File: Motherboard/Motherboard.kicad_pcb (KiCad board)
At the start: 8 copper layers, 304.8 x 243.8 mm, 110 parts, among them J1 ATX-20, J2 65SIB_Connector, J3 DB9_Header, J4 GPIO_Connector, J5 Expansion_Connector, J6 Expansion_Connector, J7 Expansion_Connector, J8 Expansion_Connector, J9 Expansion_Connector, SW1 SW_SPST, U1 74HCT138, U10 74HCT138, U11 74HCT02, U2 AS6C4008-55PCN, U3 74HCT138, U4 74HCT138, U5 74HCT138, U6 28C010, U7 74HCT08, U8 74HCT138, U9 74HCT138, X1 ACO-8MHz

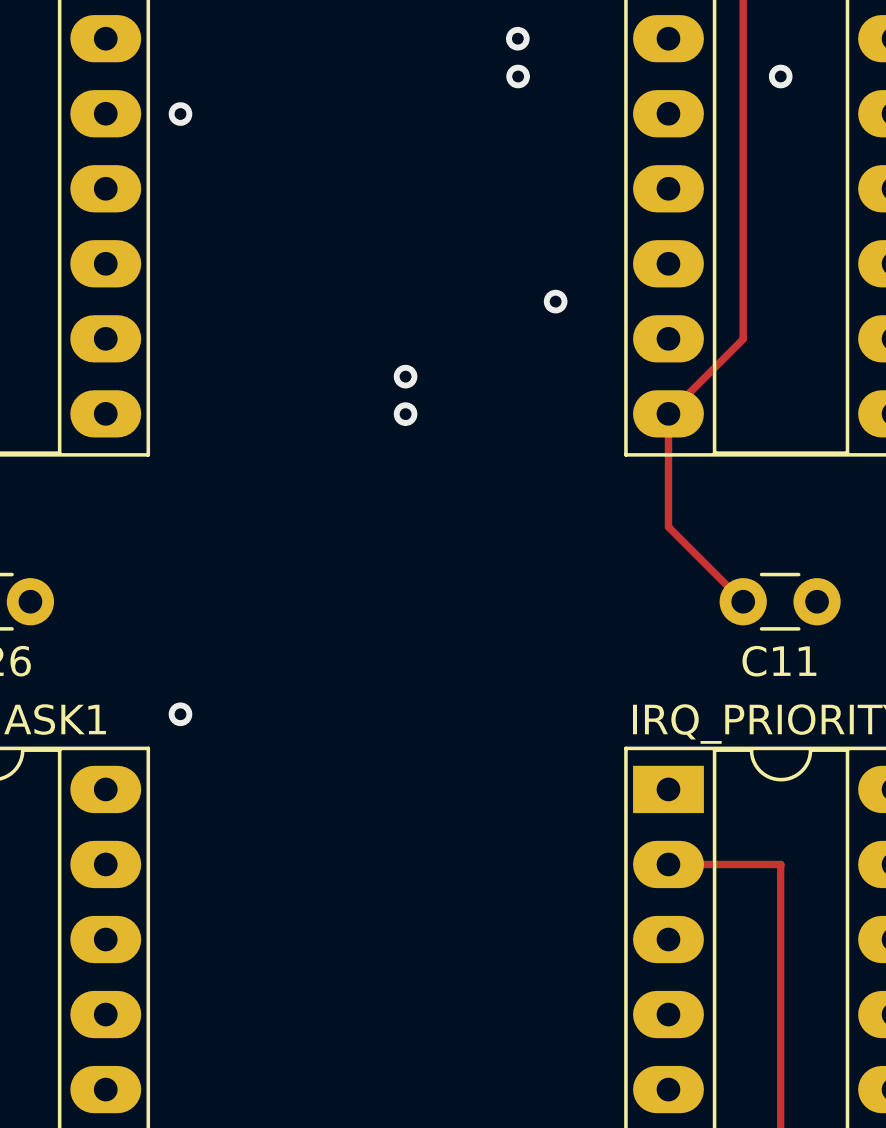
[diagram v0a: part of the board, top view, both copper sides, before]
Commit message: 247 unrouted traces...
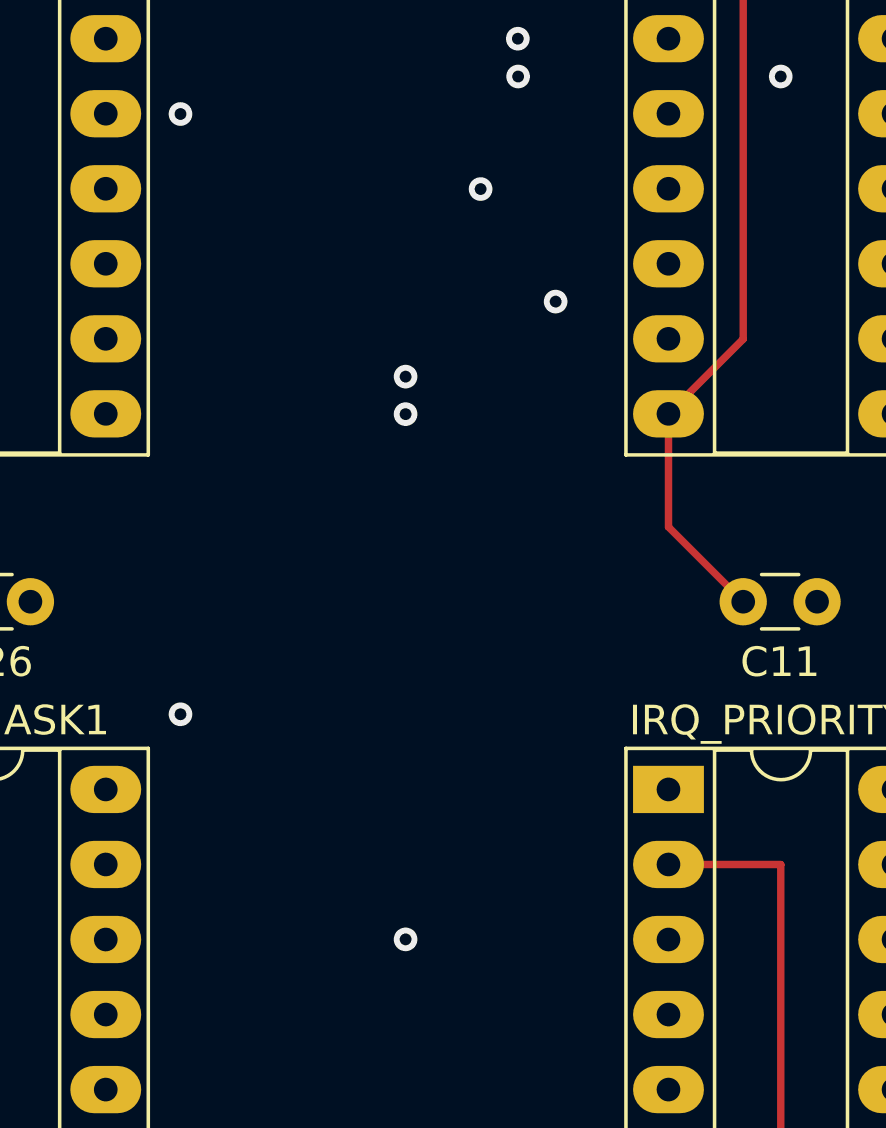
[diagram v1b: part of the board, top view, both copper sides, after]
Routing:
- net ~{IRQ2}: track 49.5 -> 214.4 mm, vias 1 -> 2
- net CS_DEV: track 231.7 -> 300.6 mm
- net 65SIB_MISO: track 0.00 -> 63.4 mm
- net 65SIB_CLK: track 0.00 -> 58.1 mm
- net 65SIB_MOSI: track 0.00 -> 53.4 mm
- net Net-(65SIB/MM1-Pad11): track 0.00 -> 31.5 mm
- net Net-(65SIB/MM1-Pad13): track 0.00 -> 31.2 mm
- net Net-(65SIB/MM1-Pad12): track 0.00 -> 31.2 mm
- net Net-(65SIB/MM1-Pad10): track 0.00 -> 31.2 mm
- net Net-(IRQ_DECODE1-Pad9): track 29.2 -> 55.9 mm, vias 2 -> 3
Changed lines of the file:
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@@
   (segment (start 133.505489 210.664511) (end 143.625489 210.664511) (width 0.25) (layer "In3.Cu") (net 1))
   (segment (start 219.705 177.8) (end 220.829511 178.924511) (width 0.25) (layer "In3.Cu") (net 1))
+  (segment (start 176.535 229.865) (end 172.87048 233.52952) (width 0.25) (layer "In5.Cu") (net 10))
+  (segment (start 148.43952 233.52952) (end 147.32 232.41) (width 0.25) (layer "In5.Cu") (net 10))
+  (segment (start 172.87048 233.52952) (end 148.43952 233.52952) (width 0.25) (layer "In5.Cu") (net 10))
+  (segment (start 147.32 229.87) (end 148.43952 230.98952) (width 0.25) (layer "In5.Cu") (net 11))
+  (segment (start 148.43952 230.98952) (end 173.420169 230.98952) (width 0.25) (layer "In5.Cu") (net 11))
+  (segment (start 176.535 227.874689) (end 176.535 227.325) (width 0.25) (layer "In5.Cu") (net 11))
+  (segment (start 173.420169 230.98952) (end 176.535 227.874689) (width 0.25) (layer "In5.Cu") (net 11))
+  (segment (start 172.87048 228.44952) (end 148.43952 228.44952) (width 0.25) (layer "In5.Cu") (net 12))
+  (segment (start 176.535 224.785) (end 172.87048 228.44952) (width 0.25) (layer "In5.Cu") (net 12))
+  (segment (start 148.43952 228.44952) (end 147.32 227.33) (width 0.25) (layer "In5.Cu") (net 12))
+  (segment (start 175.41048 221.12048) (end 150.98952 221.12048) (width 0.25) (layer "In5.Cu") (net 13))
+  (segment (start 150.98952 221.12048) (end 147.32 224.79) (width 0.25) (layer "In5.Cu") (net 13))
+  (segment (start 176.535 222.245) (end 175.41048 221.12048) (width 0.25) (layer "In5.Cu") (net 13))
   (via (at 121.92 200.66) (size 0.8) (drill 0.4) (layers "F.Cu" "B.Cu") (net 14))
   (via (at 121.92 215.9) (size 0.8) (drill 0.4) (layers "F.Cu" "B.Cu") (net 14))
@@
   (segment (start 125.73 215.9) (end 125.74 215.89) (width 0.25) (layer "In3.Cu") (net 14))
   (segment (start 121.92 215.9) (end 125.73 215.9) (width 0.25) (layer "In3.Cu") (net 14))
+  (segment (start 127.02 222.25) (end 137.709689 222.25) (width 0.25) (layer "In5.Cu") (net 15))
+  (segment (start 137.709689 222.25) (end 138.834209 221.12548) (width 0.25) (layer "In5.Cu") (net 15))
+  (segment (start 152.690961 218.44) (end 175.26 218.44) (width 0.25) (layer "In5.Cu") (net 15))
+  (segment (start 125.74 220.97) (end 127.02 222.25) (width 0.25) (layer "In5.Cu") (net 15))
+  (segment (start 175.26 218.44) (end 176.535 217.165) (width 0.25) (layer "In5.Cu") (net 15))
+  (segment (start 150.005481 221.12548) (end 152.690961 218.44) (width 0.25) (layer "In5.Cu") (net 15))
+  (segment (start 138.834209 221.12548) (end 150.005481 221.12548) (width 0.25) (layer "In5.Cu") (net 15))
+  (segment (start 178.05952 216.14952) (end 178.05952 222.710791) (width 0.25) (layer "In5.Cu") (net 16))
+  (segment (start 160.429209 223.36952) (end 157.884209 225.91452) (width 0.25) (layer "In5.Cu") (net 16))
+  (segment (start 126.914511 224.684511) (end 125.74 223.51) (width 0.25) (layer "In5.Cu") (net 16))
+  (segment (start 131.524991 224.684511) (end 126.914511 224.684511) (width 0.25) (layer "In5.Cu") (net 16))
+  (segment (start 132.755 225.91452) (end 131.524991 224.684511) (width 0.25) (layer "In5.Cu") (net 16))
+  (segment (start 157.884209 225.91452) (end 132.755 225.91452) (width 0.25) (layer "In5.Cu") (net 16))
+  (segment (start 178.05952 222.710791) (end 177.400791 223.36952) (width 0.25) (layer "In5.Cu") (net 16))
+  (segment (start 176.535 214.625) (end 178.05952 216.14952) (width 0.25) (layer "In5.Cu") (net 16))
+  (segment (start 177.400791 223.36952) (end 160.429209 223.36952) (width 0.25) (layer "In5.Cu") (net 16))
+  (segment (start 137.709689 214.63) (end 124.987507 214.63) (width 0.25) (layer "In5.Cu") (net 17))
+  (segment (start 124.987507 214.63) (end 124.46 215.157507) (width 0.25) (layer "In5.Cu") (net 17))
+  (segment (start 124.46 217.15) (end 125.74 218.43) (width 0.25) (layer "In5.Cu") (net 17))
+  (segment (start 124.46 215.157507) (end 124.46 217.15) (width 0.25) (layer "In5.Cu") (net 17))
+  (segment (start 138.834209 215.75452) (end 137.709689 214.63) (width 0.25) (layer "In5.Cu") (net 17))
+  (segment (start 172.86548 215.75452) (end 138.834209 215.75452) (width 0.25) (layer "In5.Cu") (net 17))
+  (segment (start 176.535 212.085) (end 172.86548 215.75452) (width 0.25) (layer "In5.Cu") (net 17))
   (segment (start 251.46 110.49) (end 260.35 110.49) (width 0.25) (layer "In1.Cu") (net 20))
   (segment (start 144.79 111.75) (end 144.8 111.76) (width 0.25) (layer "In1.Cu") (net 20))
@@
   (segment (start 274.32 132.08) (end 280.1275 137.8875) (width 0.25) (layer "In1.Cu") (net 20))
   (segment (start 231.14 200.62) (end 231.14 201.935) (width 0.25) (layer "In1.Cu") (net 20))
+  (via (at 158.75 53.34) (size 0.8) (drill 0.4) (layers "F.Cu" "B.Cu") (net 21))
   (via (at 111.76 54.61) (size 0.8) (drill 0.4) (layers "F.Cu" "B.Cu") (net 21))
   (segment (start 111.76 40.64) (end 111.76 54.61) (width 0.25) (layer "In2.Cu") (net 21))
+  (segment (start 158.74 53.33) (end 146.06 53.33) (width 0.25) (layer "In3.Cu") (net 21))
+  (segment (start 158.75 53.34) (end 158.74 53.33) (width 0.25) (layer "In3.Cu") (net 21))
   (segment (start 146.06 54.6) (end 146.05 54.61) (width 0.25) (layer "In3.Cu") (net 21))
   (segment (start 146.06 53.33) (end 146.06 54.6) (width 0.25) (layer "In3.Cu") (net 21))
   (segment (start 146.05 54.61) (end 111.76 54.61) (width 0.25) (layer "In3.Cu") (net 21))
+  (segment (start 158.75 201.92) (end 158.75 53.34) (width 0.25) (layer "In4.Cu") (net 21))
+  (segment (start 161.295 204.465) (end 158.75 201.92) (width 0.25) (layer "In4.Cu") (net 21))
   (via (at 287.02 255.27) (size 0.8) (drill 0.4) (layers "F.Cu" "B.Cu") (net 22))
   (via (at 255.27 105.41) (size 0.8) (drill 0.4) (layers "F.Cu" "B.Cu") (net 22))
@@
   (segment (start 153.67 219.71) (end 147.32 219.71) (width 0.25) (layer "In3.Cu") (net 23))
   (segment (start 154.94 115.57) (end 154.94 114.3) (width 0.25) (layer "In3.Cu") (net 23))
+  (segment (start 225.91952 210.66952) (end 228.595 213.345) (width 0.25) (layer "In5.Cu") (net 23))
+  (segment (start 162.41952 210.66952) (end 225.91952 210.66952) (width 0.25) (layer "In5.Cu") (net 23))
+  (segment (start 161.295 209.545) (end 162.41952 210.66952) (width 0.25) (layer "In5.Cu") (net 23))
   (via (at 185.42 96.52) (size 0.8) (drill 0.4) (layers "F.Cu" "B.Cu") (net 25))
   (via (at 232.41 60.96) (size 0.8) (drill 0.4) (layers "F.Cu" "B.Cu") (net 25))
@@
   (via (at 156.21 59.69) (size 0.8) (drill 0.4) (layers "F.Cu" "B.Cu") (net 115))
   (via (at 156.21 60.96) (size 0.8) (drill 0.4) (layers "F.Cu" "B.Cu") (net 115))
+  (via (at 156.21 78.74) (size 0.8) (drill 0.4) (layers "F.Cu" "B.Cu") (net 115))
   (segment (start 156.21 60.96) (end 156.21 59.69) (width 0.25) (layer "In2.Cu") (net 115))
+  (segment (start 156.21 78.74) (end 156.21 60.96) (width 0.25) (layer "In2.Cu") (net 115))
+  (segment (start 156.215 78.745) (end 156.21 78.74) (width 0.25) (layer "In3.Cu") (net 115))
+  (segment (start 165.11 78.745) (end 156.215 78.745) (width 0.25) (layer "In3.Cu") (net 115))
   (segment (start 172.72 59.69) (end 172.73 59.68) (width 0.25) (layer "In3.Cu") (net 115))
   (segment (start 156.2 60.95) (end 156.21 60.96) (width 0.25) (layer "In3.Cu") (net 115))

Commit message: 243 unrouted traces...
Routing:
- net 8MHz: track 57.1 -> 304.0 mm, vias 4 -> 8
- net MEM_D0: track 348.3 -> 486.7 mm, vias 2 -> 4
- net A4: track 292.1 -> 383.5 mm, vias 2 -> 3
- net A6: track 297.7 -> 371.9 mm, vias 2 -> 4
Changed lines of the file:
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@@
   (segment (start 138.44 80) (end 138.44 78.745) (width 0.25) (layer "In5.Cu") (net 32))
   (segment (start 167.63 80) (end 167.62 80.01) (width 0.25) (layer "In5.Cu") (net 32))
+  (via (at 199.39 170.18) (size 0.8) (drill 0.4) (layers "F.Cu" "B.Cu") (net 33))
+  (via (at 199.39 78.74) (size 0.8) (drill 0.4) (layers "F.Cu" "B.Cu") (net 33))
   (via (at 175.26 76.2) (size 0.8) (drill 0.4) (layers "F.Cu" "B.Cu") (net 33))
   (via (at 175.26 30.48) (size 0.8) (drill 0.4) (layers "F.Cu" "B.Cu") (net 33))
@@
   (segment (start 252.73 30.49) (end 253.904511 31.664511) (width 0.25) (layer "In2.Cu") (net 33))
   (segment (start 201.93 30.48) (end 203.295489 31.845489) (width 0.25) (layer "In2.Cu") (net 33))
+  (segment (start 199.39 78.74) (end 199.39 170.18) (width 0.25) (layer "In2.Cu") (net 33))
   (segment (start 227.33 30.49) (end 228.695489 31.855489) (width 0.25) (layer "In2.Cu") (net 33))
   (segment (start 251.364511 31.855489) (end 252.73 30.49) (width 0.25) (layer "In2.Cu") (net 33))
@@
   (segment (start 225.974511 31.845489) (end 227.33 30.49) (width 0.25) (layer "In2.Cu") (net 33))
   (segment (start 264.8875 170.18) (end 263.6175 171.45) (width 0.25) (layer "In3.Cu") (net 33))
+  (segment (start 199.39 76.2) (end 175.26 76.2) (width 0.25) (layer "In3.Cu") (net 33))
   (segment (start 220.975 171.45) (end 219.705 170.18) (width 0.25) (layer "In3.Cu") (net 33))
   (segment (start 172.73 76.205) (end 175.255 76.205) (width 0.25) (layer "In3.Cu") (net 33))
@@
   (segment (start 175.255 76.205) (end 175.26 76.2) (width 0.25) (layer "In3.Cu") (net 33))
   (segment (start 179.07 236.22) (end 162.57 236.22) (width 0.25) (layer "In3.Cu") (net 33))
+  (segment (start 199.39 78.74) (end 199.39 76.2) (width 0.25) (layer "In3.Cu") (net 33))
   (segment (start 242.70048 237.33952) (end 180.18952 237.33952) (width 0.25) (layer "In3.Cu") (net 33))
   (segment (start 263.6175 171.45) (end 220.975 171.45) (width 0.25) (layer "In3.Cu") (net 33))
@@
   (segment (start 175.26 30.48) (end 201.93 30.48) (width 0.25) (layer "In3.Cu") (net 33))
   (segment (start 243.835 236.205) (end 242.70048 237.33952) (width 0.25) (layer "In3.Cu") (net 33))
+  (segment (start 199.39 170.18) (end 219.705 170.18) (width 0.25) (layer "In3.Cu") (net 33))
   (segment (start 138.44 76.205) (end 138.44 77.46) (width 0.25) (layer "In5.Cu") (net 33))
   (segment (start 172.73 77.46) (end 172.73 76.205) (width 0.25) (layer "In5.Cu") (net 33))
@@
   (segment (start 83.815 205.735) (end 83.82 205.74) (width 0.25) (layer "In3.Cu") (net 52))
   (segment (start 85.09 209.55) (end 102.87 209.55) (width 0.25) (layer "F.Cu") (net 53))
+  (via (at 114.3 209.55) (size 0.8) (drill 0.4) (layers "F.Cu" "B.Cu") (net 53))
+  (via (at 186.69 64.77) (size 0.8) (drill 0.4) (layers "F.Cu" "B.Cu") (net 53))
   (via (at 85.09 209.55) (size 0.8) (drill 0.4) (layers "F.Cu" "B.Cu") (net 53))
+  (via (at 115.57 64.77) (size 0.8) (drill 0.4) (layers "F.Cu" "B.Cu") (net 53))
+  (via (at 186.69 60.96) (size 0.8) (drill 0.4) (layers "F.Cu" "B.Cu") (net 53))
   (via (at 85.09 208.28) (size 0.8) (drill 0.4) (layers "F.Cu" "B.Cu") (net 53))
   (via (at 85.09 226.06) (size 0.8) (drill 0.4) (layers "F.Cu" "B.Cu") (net 53))
   (via (at 102.87 209.55) (size 0.8) (drill 0.4) (layers "F.Cu" "B.Cu") (net 53))
   (segment (start 102.87 199.39) (end 102.87 209.55) (width 0.25) (layer "In2.Cu") (net 53))
+  (segment (start 186.69 64.77) (end 186.69 60.96) (width 0.25) (layer "In2.Cu") (net 53))
+  (segment (start 114.3 209.55) (end 115.57 208.28) (width 0.25) (layer "In2.Cu") (net 53))
+  (segment (start 115.57 208.28) (end 115.57 64.77) (width 0.25) (layer "In2.Cu") (net 53))
   (segment (start 85.09 226.06) (end 85.09 208.28) (width 0.25) (layer "In2.Cu") (net 53))
+  (segment (start 102.87 209.55) (end 114.3 209.55) (width 0.25) (layer "In3.Cu") (net 53))
   (segment (start 85.09 208.28) (end 85.085 208.275) (width 0.25) (layer "In3.Cu") (net 53))
+  (segment (start 115.57 64.77) (end 186.69 64.77) (width 0.25) (layer "In3.Cu") (net 53))
   (segment (start 85.085 208.275) (end 81.29 208.275) (width 0.25) (layer "In3.Cu") (net 53))
+  (segment (start 186.69 60.96) (end 201.93 60.96) (width 0.25) (layer "In3.Cu") (net 53))
   (segment (start 92.71 226.06) (end 85.09 226.06) (width 0.25) (layer "In3.Cu") (net 53))
   (via (at 101.6 194.31) (size 0.8) (drill 0.4) (layers "F.Cu" "B.Cu") (net 54))
@@
   (via (at 224.79 160.02) (size 0.8) (drill 0.4) (layers "F.Cu" "B.Cu") (net 64))
   (via (at 314.96 158.75) (size 0.8) (drill 0.4) (layers "F.Cu" "B.Cu") (net 64))
+  (via (at 154.94 157.48) (size 0.8) (drill 0.4) (layers "F.Cu" "B.Cu") (net 64))
   (segment (start 281.955 46.99) (end 280.67 45.705) (width 0.25) (layer "In2.Cu") (net 64))
+  (segment (start 154.95 157.49) (end 154.95 184.16) (width 0.25) (layer "In2.Cu") (net 64))
   (segment (start 229.87 45.73) (end 228.61 46.99) (width 0.25) (layer "In2.Cu") (net 64))
   (segment (start 228.61 46.99) (end 205.74 46.99) (width 0.25) (layer "In2.Cu") (net 64))
@@
   (segment (start 314.97 158.76) (end 314.96 158.75) (width 0.25) (layer "In2.Cu") (net 64))
   (segment (start 205.74 46.99) (end 204.47 45.72) (width 0.25) (layer "In2.Cu") (net 64))
+  (segment (start 154.94 157.48) (end 154.95 157.49) (width 0.25) (layer "In2.Cu") (net 64))
   (segment (start 305.25 46.99) (end 281.955 46.99) (width 0.25) (layer "In2.Cu") (net 64))
   (segment (start 255.27 45.73) (end 254.01 46.99) (width 0.25) (layer "In2.Cu") (net 64))
@@
   (segment (start 314.97 210.83) (end 314.97 158.76) (width 0.25) (layer "In2.Cu") (net 64))
   (segment (start 256.515 46.975) (end 255.27 45.73) (width 0.25) (layer "In2.Cu") (net 64))
+  (segment (start 219.705 157.48) (end 154.94 157.48) (width 0.25) (layer "In3.Cu") (net 64))
   (segment (start 220.829511 158.604511) (end 224.935489 158.604511) (width 0.25) (layer "In3.Cu") (net 64))
   (segment (start 266.1575 158.75) (end 314.96 158.75) (width 0.25) (layer "In3.Cu") (net 64))
@@
   (segment (start 152.41 184.16) (end 152.41 181.62) (width 0.25) (layer "In5.Cu") (net 65))
   (segment (start 152.41 181.62) (end 152.43 181.6) (width 0.25) (layer "In5.Cu") (net 65))
+  (via (at 149.86 181.61) (size 0.8) (drill 0.4) (layers "F.Cu" "B.Cu") (net 66))
+  (via (at 220.98 180.34) (size 0.8) (drill 0.4) (layers "F.Cu" "B.Cu") (net 66))
   (via (at 221.104503 154.94) (size 0.8) (drill 0.4) (layers "F.Cu" "B.Cu") (net 66))
   (via (at 309.88 153.67) (size 0.8) (drill 0.4) (layers "F.Cu" "B.Cu") (net 66))
@@
   (segment (start 254.01 52.07) (end 231.13 52.07) (width 0.25) (layer "In2.Cu") (net 66))
   (segment (start 205.74 52.07) (end 204.47 50.8) (width 0.25) (layer "In2.Cu") (net 66))
+  (segment (start 149.87 181.62) (end 149.86 181.61) (width 0.25) (layer "In2.Cu") (net 66))
+  (segment (start 149.87 184.16) (end 149.87 181.62) (width 0.25) (layer "In2.Cu") (net 66))
   (segment (start 229.87 50.81) (end 228.61 52.07) (width 0.25) (layer "In2.Cu") (net 66))
   (segment (start 221.125489 154.919014) (end 221.125489 153.524511) (width 0.25) (layer "In3.Cu") (net 66))
+  (segment (start 149.86 181.61) (end 219.71 181.61) (width 0.25) (layer "In3.Cu") (net 66))
   (segment (start 266.1575 153.67) (end 309.88 153.67) (width 0.25) (layer "In3.Cu") (net 66))
   (segment (start 219.705 152.4) (end 220.829511 153.524511) (width 0.25) (layer "In3.Cu") (net 66))
   (segment (start 220.829511 153.524511) (end 221.125489 153.524511) (width 0.25) (layer "In3.Cu") (net 66))
+  (segment (start 219.71 181.61) (end 220.98 180.34) (width 0.25) (layer "In3.Cu") (net 66))
   (segment (start 221.125489 153.524511) (end 263.762989 153.524511) (width 0.25) (layer "In3.Cu") (net 66))
   (segment (start 264.8875 152.4) (end 266.1575 153.67) (width 0.25) (layer "In3.Cu") (net 66))
@@
   (segment (start 263.762989 153.524511) (end 264.8875 152.4) (width 0.25) (layer "In3.Cu") (net 66))
   (segment (start 219.72 195.59) (end 219.72 181.6) (width 0.25) (layer "In4.Cu") (net 66))
-  (segment (start 219.72 181.6) (end 221.104503 180.215497) (width 0.25) (layer "In4.Cu") (net 66))
+  (segment (start 220.98 180.34) (end 221.104503 180.215497) (width 0.25) (layer "In4.Cu") (net 66))
   (segment (start 221.104503 180.215497) (end 221.104503 154.94) (width 0.25) (layer "In4.Cu") (net 66))
+  (segment (start 219.72 181.6) (end 220.98 180.34) (width 0.25) (layer "In4.Cu") (net 66))
   (via (at 304.8 151.13) (size 0.8) (drill 0.4) (layers "F.Cu" "B.Cu") (net 67))
   (via (at 214.63 185.42) (size 0.8) (drill 0.4) (layers "F.Cu" "B.Cu") (net 67))

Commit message: 239 unrouted traces...
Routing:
- net A5: track 366.9 -> 509.9 mm, vias 3 -> 6
- net A4: track 383.5 -> 522.7 mm, vias 3 -> 6
- net A6: track 371.9 -> 509.8 mm, vias 4 -> 7
- net A7: track 376.3 -> 509.1 mm, vias 3 -> 6

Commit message: 233 unrouted traces...
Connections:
- CLK_DIV1 pad 14: (no net) -> VCC
- CLK_DIV1 pad 7: (no net) -> GND
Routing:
- net A3: track 238.5 -> 470.4 mm, vias 2 -> 5
- net A2: track 235.0 -> 374.2 mm, vias 2 -> 4
- net GND: track 1839.4 -> 1925.8 mm
- net A4: track 522.7 -> 581.1 mm, vias 6 -> 7
- net VCC: track 1649.6 -> 1651.1 mm
